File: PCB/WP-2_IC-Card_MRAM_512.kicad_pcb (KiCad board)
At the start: 2 copper layers, 54 x 54 mm, 21 parts, among them J1 SMS-138-01-G-S, SW1 CUS-14TB, U1 MR2A08xxYSxxx, U2 16827, U3 8T245, U4 MIC5317-3.3YD5, U5 2G32

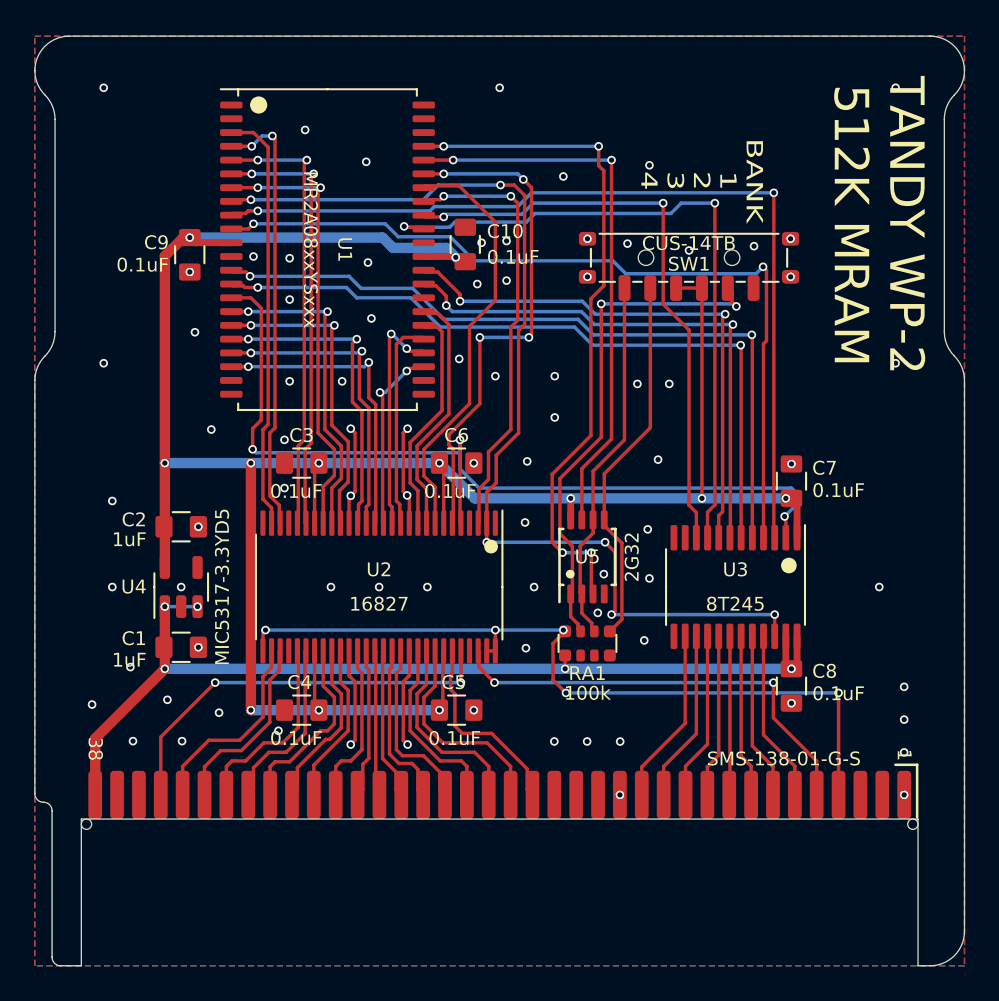
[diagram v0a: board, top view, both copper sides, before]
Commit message: mram 512 level-shift parts, battery backed ram top cover
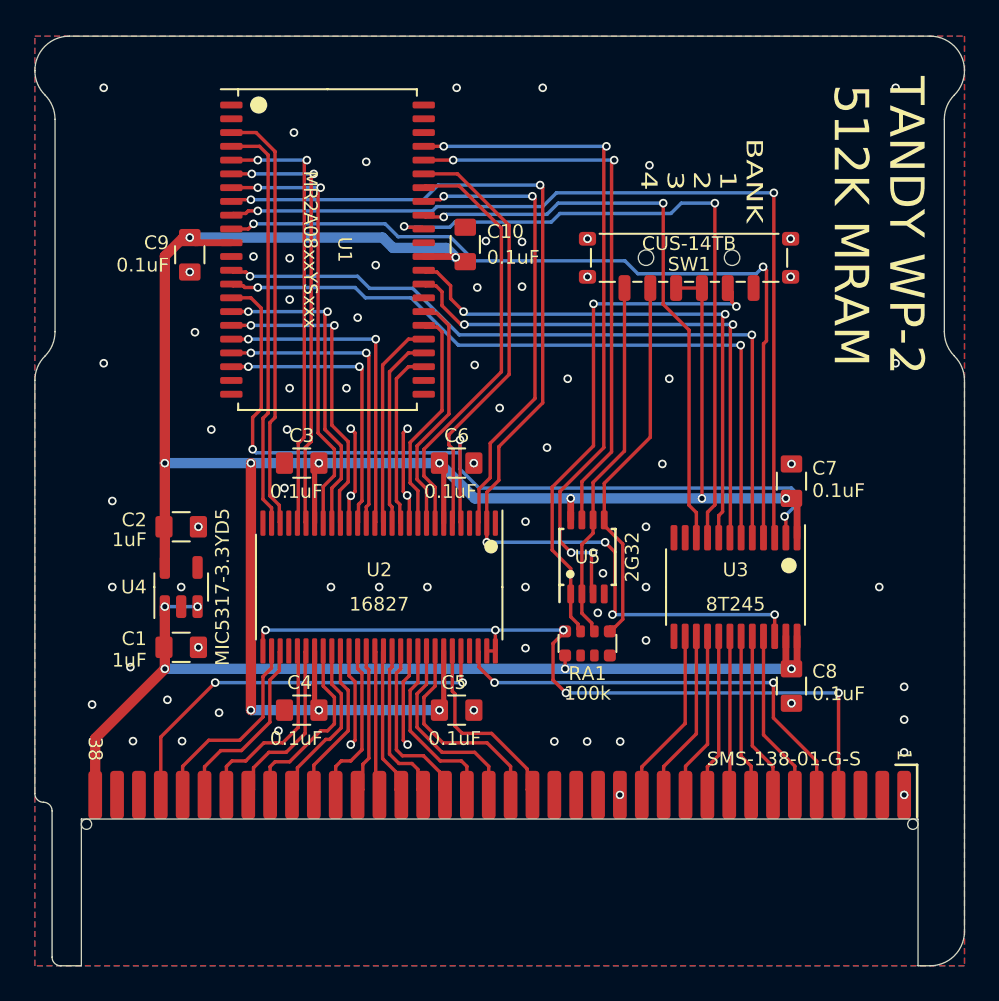
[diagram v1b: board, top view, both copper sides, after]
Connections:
- U1 pad 18: /3A7 -> /3A9
- U1 pad 20: /3A9 -> /3A7
- U1 pad 25: /3A10 -> /3A12
- U1 pad 27: /3A12 -> /3A10
- U1 pad 3: /3A0 -> /3A1
- U1 pad 4: /3A1 -> /3A0
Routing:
- net /3A16: track 29.9 -> 25.1 mm, vias 4 -> 0
- net /3A11: track 13.4 -> 11.3 mm, vias 2 -> 0
- net /3A12: track 12.3 -> 10.4 mm
- net /3A7: track 18.4 -> 16.7 mm
- net /~{3CE1}: track 60.9 -> 62.6 mm
- net /~{3OE}: track 25.3 -> 26.9 mm
- net /3A9: track 17.6 -> 19.1 mm
- net /3A10: track 10.9 -> 12.2 mm, vias 2 -> 0
- net /3A1: track 25.6 -> 25.0 mm, vias 2 -> 0
- net /3A0: track 24.7 -> 24.1 mm
- net /BANK_2: track 29.8 -> 30.3 mm
- net GND: vias 82 -> 77

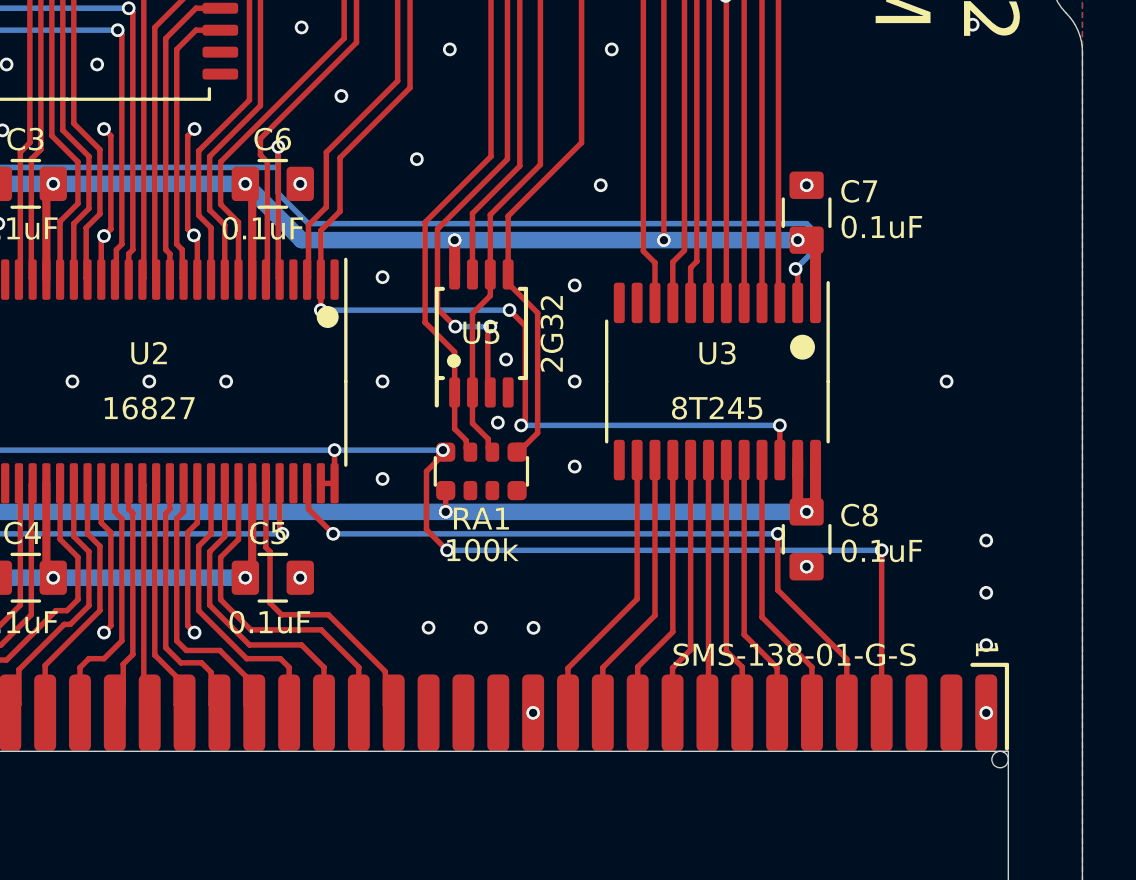
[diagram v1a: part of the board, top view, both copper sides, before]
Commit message: MRAM_512 pullups on /3CE1 /3WE
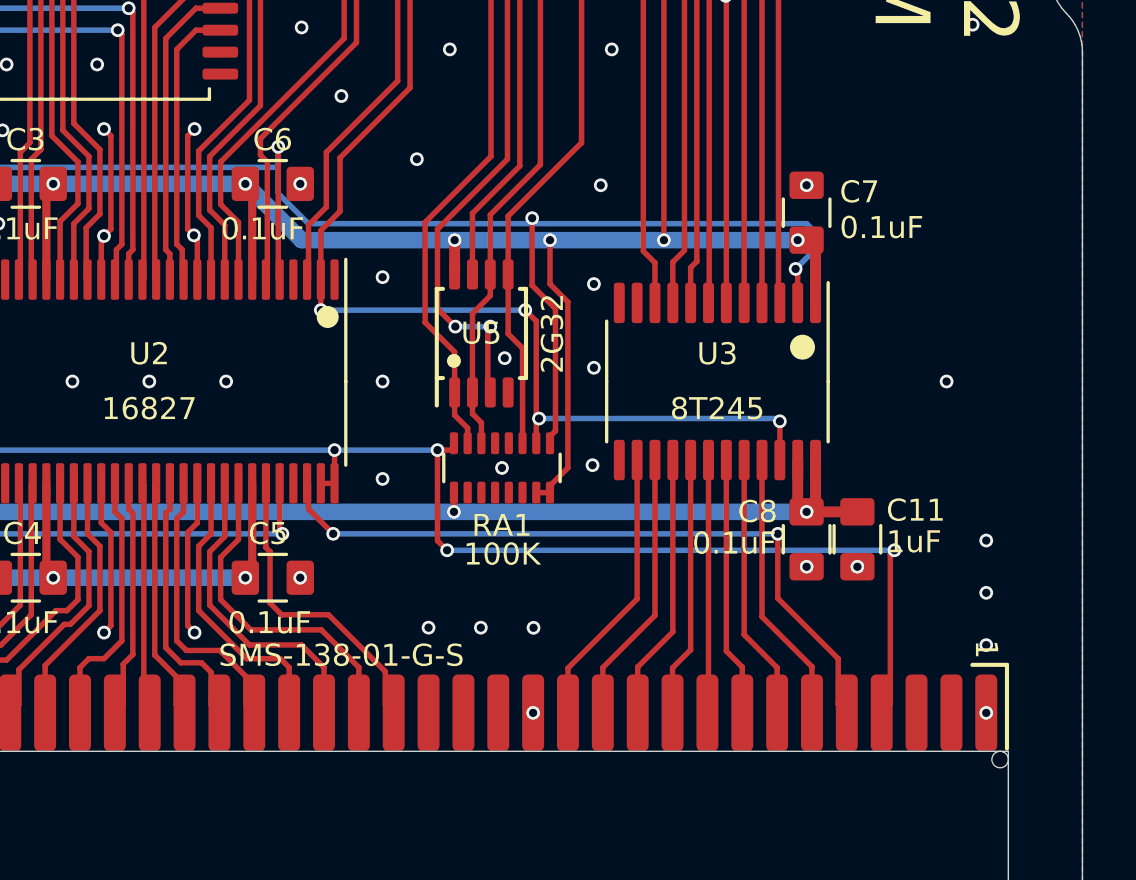
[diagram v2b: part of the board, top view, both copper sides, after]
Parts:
- added C11: 1uF, 0_LOCAL:C_0805_1mm, F.Cu at (154.8, 106.0)
- RA1: value 100k -> 100K; footprint 0_LOCAL:R_Array_Convex_4x0612 -> 0_LOCAL:R_Array_Convex_8x0602
- moved RA1 0.76 mm to (141.8, 103.4), turned to 90 degrees
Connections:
- RA1 pad 1: /BANK_3 -> VBUS
- RA1 pad 2: /BANK_4 -> GND
- RA1 pad 3: /BANK_2 -> GND
- RA1 pad 4: /~{CE1} -> GND
- RA1 pad 5: VBUS -> GND
- RA1 pad 7: GND -> VMEM
- RA1 pad 8: GND -> VMEM
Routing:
- net VMEM: track 135.3 -> 145.5 mm, vias 12 -> 13
- net /~{3WE}: track 52.2 -> 61.0 mm, vias 3 -> 4
- net VBUS: track 55.7 -> 57.5 mm
- net /BANK_3: track 22.0 -> 20.9 mm
- net /~{CE1}: track 46.4 -> 47.2 mm
- net /~{3CE1}: track 62.6 -> 63.3 mm
- net GND: vias 77 -> 78
